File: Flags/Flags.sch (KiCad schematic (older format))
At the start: 35 parts, among them J1 Conn_01x09_Male, J2 Conn_01x12_Male, J3 Conn_01x04_Male, U1 74HC74, U2 74HC74, U3 74LS08, U4 74LS175, U5 74LS08

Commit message: Place ICs on Flags pcb
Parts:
- removed J2: Conn_01x12_Male, Connector_PinHeader_2.54mm:PinHeader_1x12_P2.54mm_Vertical, symbol Connector:Conn_01x12_Male
- added J2: Conn_01x07_Male, Connector_PinHeader_2.54mm:PinHeader_1x07_P2.54mm_Vertical, symbol Connector:Conn_01x07_Male
- added J4: Conn_01x05_Male, Connector_PinHeader_2.54mm:PinHeader_1x05_P2.54mm_Vertical, symbol Connector:Conn_01x05_Male
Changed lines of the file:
@@
-	1    0    0    -1
-$EndComp
-$Comp
-L Connector:Conn_01x12_Male J2
-U 1 1 62C30518
-P 1000 2750
-F 0 "J2" H 1075 3350 50  0000 C CNN
-F 1 "Conn_01x12_Male" H 875 2050 50  0000 C CNN
-F 2 "Connector_PinHeader_2.54mm:PinHeader_1x12_P2.54mm_Vertical" H 1000 2750 50  0001 C CNN
-F 3 "~" H 1000 2750 50  0001 C CNN
-	1    1000 2750
 	1    0    0    -1
 $EndComp
 Text Label 1200 2250 0    50   ~ 0
 CF_IN
+Text Label 1200 3400 0    50   ~ 0
+CF_EN
 Text Label 1200 2350 0    50   ~ 0
-CF_EN
+SF_IN
+Text Label 1200 3500 0    50   ~ 0
+SF_EN
 Text Label 1200 2450 0    50   ~ 0
-SF_IN
+ZF_IN
+Text Label 1200 3600 0    50   ~ 0
+ZF_EN
 Text Label 1200 2550 0    50   ~ 0
-SF_EN
+BF_IN
+Text Label 1200 3700 0    50   ~ 0
+BF_EN
+Text Label 1200 3800 0    50   ~ 0
+CMP_EN
 Text Label 1200 2650 0    50   ~ 0
-ZF_IN
+LT_IN
 Text Label 1200 2750 0    50   ~ 0
-ZF_EN
+~EQ_IN
 Text Label 1200 2850 0    50   ~ 0
-BF_IN
-Text Label 1200 2950 0    50   ~ 0
-BF_EN
-Text Label 1200 3350 0    50   ~ 0
-CMP_EN
-Text Label 1200 3050 0    50   ~ 0
-LT_IN
-Text Label 1200 3150 0    50   ~ 0
-~EQ_IN
-Text Label 1200 3250 0    50   ~ 0
 GT_IN
 $Comp
@@
 	1    0    0    -1
 $EndComp
+$Comp
+L Connector:Conn_01x05_Male J4
+U 1 1 62B6C12E
+P 1000 3600
+F 0 "J4" H 1108 3981 50  0000 C CNN
+F 1 "Conn_01x05_Male" H 1075 3325 50  0000 C CNN
+F 2 "Connector_PinHeader_2.54mm:PinHeader_1x05_P2.54mm_Vertical" H 1000 3600 50  0001 C CNN
+F 3 "~" H 1000 3600 50  0001 C CNN
+	1    1000 3600
+	1    0    0    -1
+$EndComp
+$Comp
+L Connector:Conn_01x07_Male J2
+U 1 1 62B72967
+P 1000 2550
+F 0 "J2" H 1108 3031 50  0000 C CNN
+F 1 "Conn_01x07_Male" H 1050 2175 50  0000 C CNN
+F 2 "Connector_PinHeader_2.54mm:PinHeader_1x07_P2.54mm_Vertical" H 1000 2550 50  0001 C CNN
+F 3 "~" H 1000 2550 50  0001 C CNN
+	1    1000 2550
+	1    0    0    -1
+$EndComp

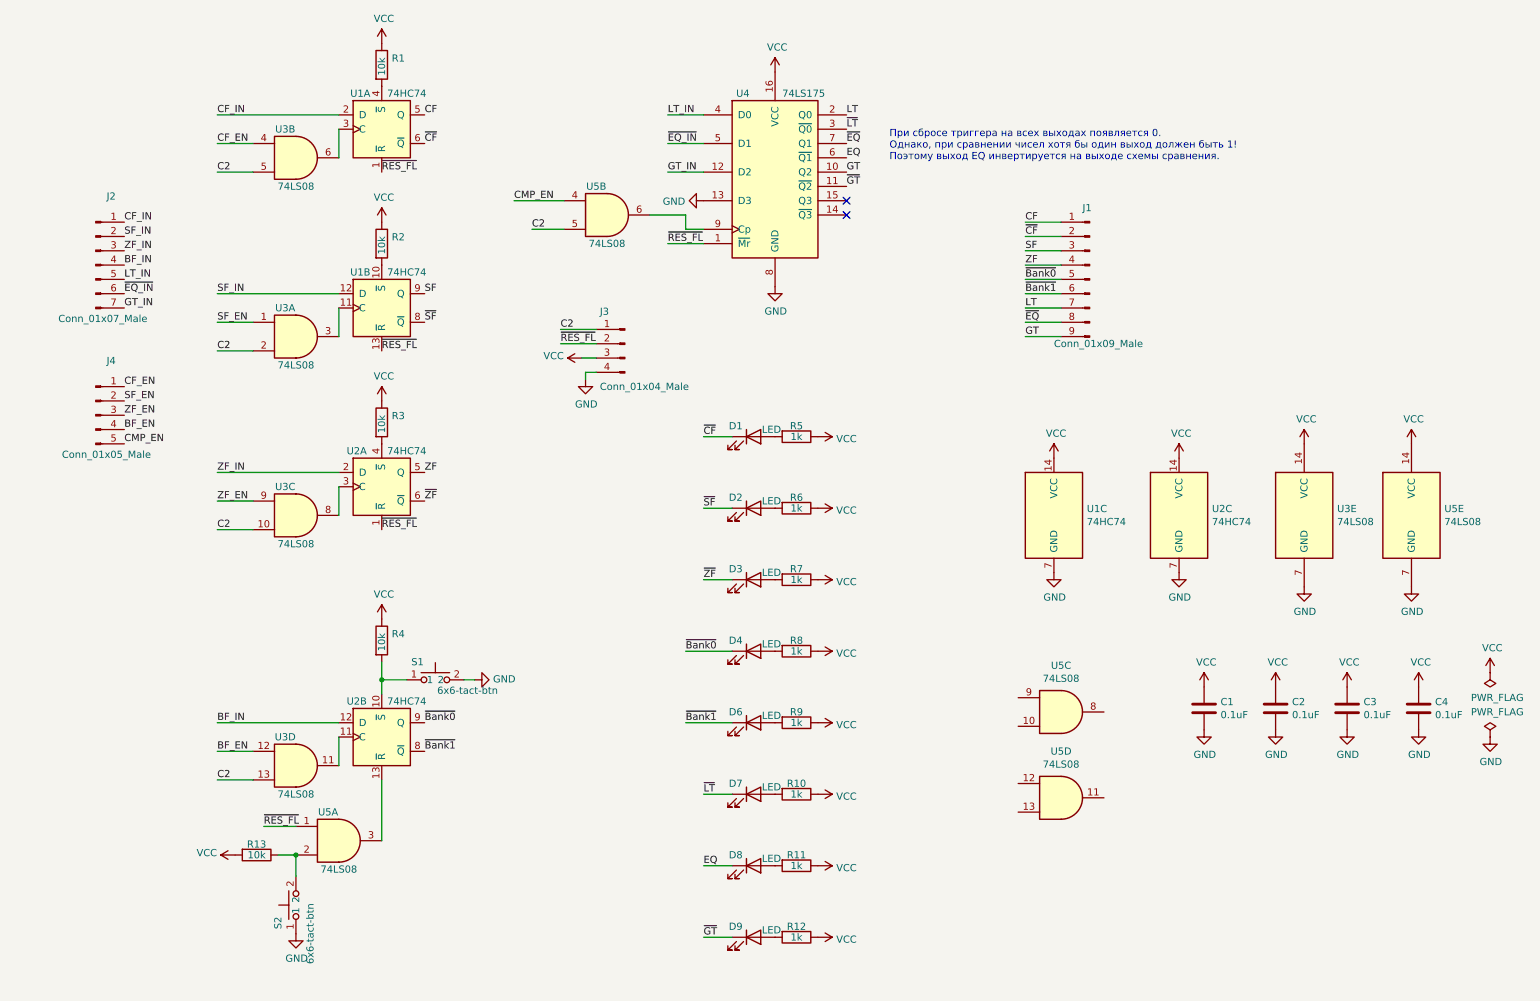
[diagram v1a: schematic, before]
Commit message: Remove some flags, fix board size
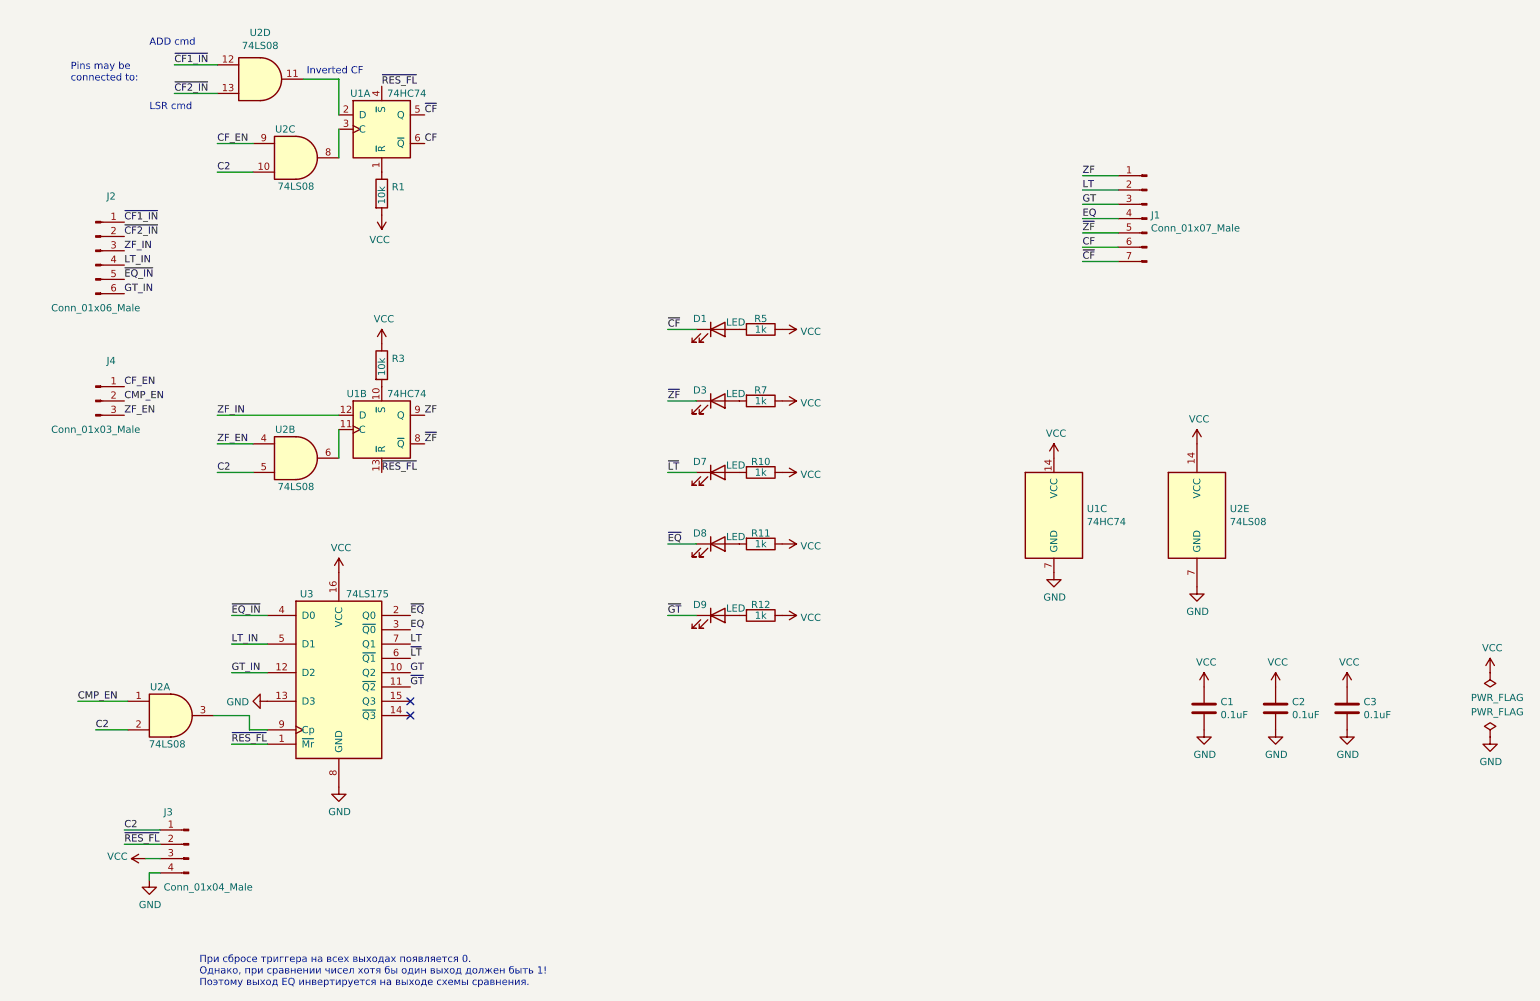
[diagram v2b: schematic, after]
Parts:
- removed C4: 0.1uF, Capacitor_THT:C_Disc_D5.0mm_W2.5mm_P5.00mm, symbol Device:C
- removed D2, D4, D6: LED, LED_THT:LED_Rectangular_W5.0mm_H2.0mm, symbol Device:LED
- removed J1: Conn_01x09_Male, Connector_PinHeader_2.54mm:PinHeader_1x09_P2.54mm_Vertical, symbol Connector:Conn_01x09_Male
- removed J2: Conn_01x07_Male, Connector_PinHeader_2.54mm:PinHeader_1x07_P2.54mm_Vertical, symbol Connector:Conn_01x07_Male
- removed J4: Conn_01x05_Male, Connector_PinHeader_2.54mm:PinHeader_1x05_P2.54mm_Vertical, symbol Connector:Conn_01x05_Male
- removed R13, R2, R4: 10k, Resistor_SMD:R_0805_2012Metric_Pad1.20x1.40mm_HandSolder, symbol Device:R
- removed R6, R8, R9: 1k, Resistor_SMD:R_0805_2012Metric_Pad1.20x1.40mm_HandSolder, symbol Device:R
- removed S1, S2: 6x6-tact-btn, Button_Switch_THT:SW_PUSH_6mm_H4.3mm, symbol CommonLibrary:6x6-tact-btn
- removed U2: 74HC74, Package_DIP:DIP-14_W7.62mm_Socket, symbol 74xx:74HC74
- removed unit 1 of U3
- removed unit 4 of U3
- removed unit 5 of U3
- removed unit 1 of U5
- removed unit 2 of U5
- removed unit 3 of U5
- removed unit 4 of U5
- added J1: Conn_01x07_Male, Connector_PinHeader_2.54mm:PinHeader_1x07_P2.54mm_Vertical, symbol Connector:Conn_01x07_Male
- added J2: Conn_01x06_Male, Connector_PinHeader_2.54mm:PinHeader_1x06_P2.54mm_Vertical, symbol Connector:Conn_01x06_Male
- added J4: Conn_01x03_Male, Connector_PinHeader_2.54mm:PinHeader_1x03_P2.54mm_Vertical, symbol Connector:Conn_01x03_Male
- added unit 1 of U2
- added unit 4 of U2
- renumbered U3 to U2, U5 to U2, U4 to U3
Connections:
- net SF is gone; now on net ZF: U1.9 (Q)
- net SF_IN is gone; now on net ZF_IN: U1.12 (D)
- net ~SF is gone; now on net ~ZF: U1.8 (~Q)
- net C2: now also U2.2
- net CF: now also U1.6 (~Q), J1.6 (Pin_6); no longer U1.5 (Q)
- net CF_EN: now also U2.9, J4.1 (Pin_1); no longer U2.4
- net CMP_EN: now also J4.2 (Pin_2), U2.1
- net EQ: now also U3.3 (~Q0), J1.4 (Pin_4); no longer D8.1 (K), U3.6 (~Q1)
- net GT: now also J1.3 (Pin_3)
- net GT_IN: now also J2.6 (Pin_6)
- net LT: now also U3.7 (Q1), J1.2 (Pin_2); no longer U3.2 (Q0)
- net LT_IN: now also U3.5 (D1), J2.4 (Pin_4); no longer U3.4 (D0)
- net VCC: now also R1.2; no longer R1.1
- net ZF: now also J1.1 (Pin_1)
- net ZF_EN: now also U2.4, J4.3 (Pin_3); no longer U2.9
- net ZF_IN: now also J2.3 (Pin_3)
- net ~CF: now also U1.5 (Q), J1.7 (Pin_7); no longer U1.6 (~Q)
- net ~EQ: now also D8.1 (K), U3.2 (Q0); no longer U3.7 (Q1)
- net ~EQ_IN: now also U3.4 (D0), J2.5 (Pin_5); no longer U3.5 (D1)
- net ~LT: now also U3.6 (~Q1); no longer U3.3 (~Q0)
- net ~RES_FL: now also U1.4 (~S); no longer U1.1 (~R)
- net ~ZF: now also J1.5 (Pin_5)
- net at U1.3 (C): now also U2.8; no longer U2.6
- net at U1.10 (~S): now also R3.2
- net at U1.11 (C): now also U2.6
- net at U3.9 (Cp): now also U2.3
- net CF_IN: no longer names the net of U1.2 (D)
- net CF_IN: now also U2.11
- new net: R1.1, U1.1 (~R)
- new net ~CF1_IN: J2.1 (Pin_1), U2.12
- new net ~CF2_IN: J2.2 (Pin_2), U2.13
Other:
- note added: "ADD cmd"
- note added: "Inverted CF"
- note added: "LSR cmd"
- note added: "Pins may be\nconnected to:"
- moved on the sheet: D1, D3, D7, D8, D9, J3, R1, R10, R11, R12, R3, R5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

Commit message: Flags pcb is ready
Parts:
- C1, C2: footprint Capacitor_THT:C_Disc_D5.0mm_W2.5mm_P5.00mm -> Capacitor_THT:C_Axial_L5.1mm_D3.1mm_P12.50mm_Horizontal
- C3: footprint Capacitor_THT:C_Disc_D5.0mm_W2.5mm_P5.00mm -> Capacitor_THT:C_Axial_L5.1mm_D3.1mm_P15.00mm_Horizontal
- R1, R3: footprint Resistor_SMD:R_0805_2012Metric_Pad1.20x1.40mm_HandSolder -> Resistor_THT:R_Axial_DIN0207_L6.3mm_D2.5mm_P7.62mm_Horizontal
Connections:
- net C2: now also J3.2 (Pin_2); no longer J3.1 (Pin_1)
- net LT_IN: now also J2.5 (Pin_5); no longer J2.4 (Pin_4)
- net ~CF: now also J1.5 (Pin_5); no longer J1.7 (Pin_7)
- net ~EQ_IN: now also J2.4 (Pin_4); no longer J2.5 (Pin_5)
- net ~RES_FL: now also J3.1 (Pin_1); no longer J3.2 (Pin_2)
- net ~ZF: now also J1.7 (Pin_7); no longer J1.5 (Pin_5)
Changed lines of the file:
@@
 F 0 "R1" H 3070 2096 50  0000 L CNN
 F 1 "10k" V 3000 1975 50  0000 L CNN
-F 2 "Resistor_SMD:R_0805_2012Metric_Pad1.20x1.40mm_HandSolder" V 2930 2050 50  0001 C CNN
+F 2 "Resistor_THT:R_Axial_DIN0207_L6.3mm_D2.5mm_P7.62mm_Horizontal" V 2930 2050 50  0001 C CNN
 F 3 "~" H 3000 2050 50  0001 C CNN
 	1    3000 2050
@@
 F 0 "R3" H 3070 3296 50  0000 L CNN
 F 1 "10k" V 3000 3175 50  0000 L CNN
-F 2 "Resistor_SMD:R_0805_2012Metric_Pad1.20x1.40mm_HandSolder" V 2930 3250 50  0001 C CNN
+F 2 "Resistor_THT:R_Axial_DIN0207_L6.3mm_D2.5mm_P7.62mm_Horizontal" V 2930 3250 50  0001 C CNN
 F 3 "~" H 3000 3250 50  0001 C CNN
 	1    3000 3250
@@
 F 0 "C1" H 8865 5696 50  0000 L CNN
 F 1 "0.1uF" H 8865 5605 50  0000 L CNN
-F 2 "Capacitor_THT:C_Disc_D5.0mm_W2.5mm_P5.00mm" H 8788 5500 50  0001 C CNN
+F 2 "Capacitor_THT:C_Axial_L5.1mm_D3.1mm_P12.50mm_Horizontal" H 8788 5500 50  0001 C CNN
 F 3 "~" H 8750 5650 50  0001 C CNN
 	1    8750 5650
@@
 F 0 "C2" H 9365 5696 50  0000 L CNN
 F 1 "0.1uF" H 9365 5605 50  0000 L CNN
-F 2 "Capacitor_THT:C_Disc_D5.0mm_W2.5mm_P5.00mm" H 9288 5500 50  0001 C CNN
+F 2 "Capacitor_THT:C_Axial_L5.1mm_D3.1mm_P12.50mm_Horizontal" H 9288 5500 50  0001 C CNN
 F 3 "~" H 9250 5650 50  0001 C CNN
 	1    9250 5650
@@
 F 0 "C3" H 9865 5696 50  0000 L CNN
 F 1 "0.1uF" H 9865 5605 50  0000 L CNN
-F 2 "Capacitor_THT:C_Disc_D5.0mm_W2.5mm_P5.00mm" H 9788 5500 50  0001 C CNN
+F 2 "Capacitor_THT:C_Axial_L5.1mm_D3.1mm_P15.00mm_Horizontal" H 9788 5500 50  0001 C CNN
 F 3 "~" H 9750 5650 50  0001 C CNN
 	1    9750 5650
@@
 Text Label 1200 3500 0    50   ~ 0
 CMP_EN
+Text Label 1200 2650 0    50   ~ 0
+LT_IN
 Text Label 1200 2550 0    50   ~ 0
-LT_IN
-Text Label 1200 2650 0    50   ~ 0
 ~EQ_IN
 Text Label 1200 2750 0    50   ~ 0
@@
 Text Label 7900 2425 0    50   ~ 0
 CF
-Text Label 7900 2525 0    50   ~ 0
+Text Label 7900 2325 0    50   ~ 0
 ~CF
 Text Label 7900 1925 0    50   ~ 0
@@
 Wire Wire Line
 	1200 6600 1450 6600
+Text Label 1200 6600 0    50   ~ 0
+C2
 Text Label 1200 6500 0    50   ~ 0
-C2
-Text Label 1200 6600 0    50   ~ 0
 ~RES_FL
 $Comp
@@
 	1    0    0    -1
 $EndComp
-Text Label 7900 2325 0    50   ~ 0
+Text Label 7900 2525 0    50   ~ 0
 ~ZF
 $Comp

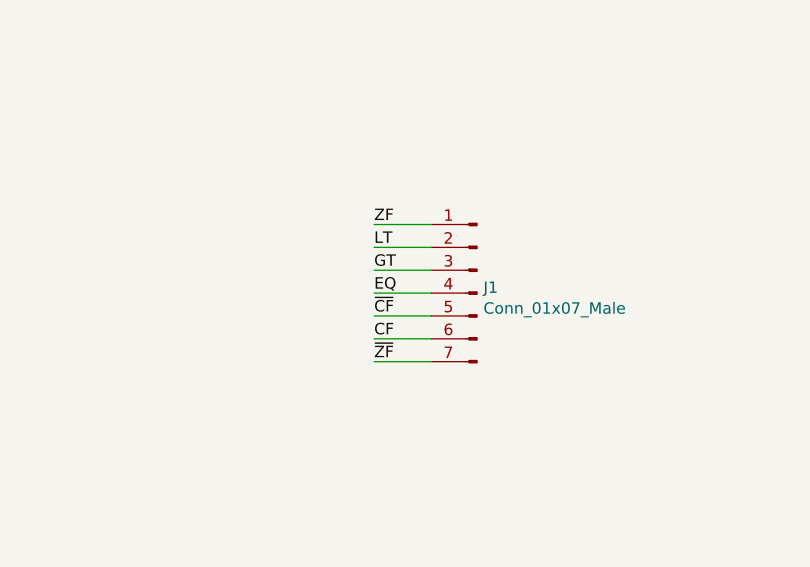
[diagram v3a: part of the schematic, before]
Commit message: Move ZF output to another place
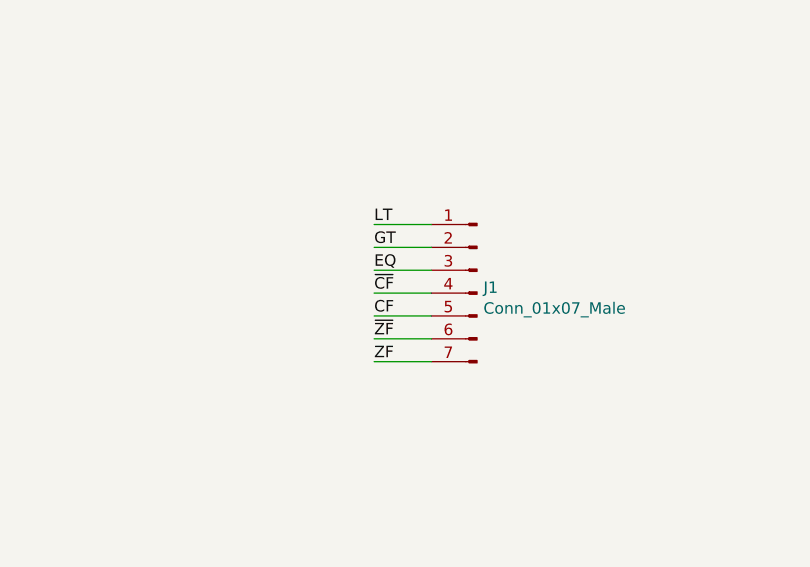
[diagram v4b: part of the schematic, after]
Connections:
- net CF: now also J1.5 (Pin_5); no longer J1.6 (Pin_6)
- net EQ: now also J1.3 (Pin_3); no longer J1.4 (Pin_4)
- net GT: now also J1.2 (Pin_2); no longer J1.3 (Pin_3)
- net LT: now also J1.1 (Pin_1); no longer J1.2 (Pin_2)
- net ZF: now also J1.7 (Pin_7); no longer J1.1 (Pin_1)
- net ~CF: now also J1.4 (Pin_4); no longer J1.5 (Pin_5)
- net ~ZF: now also J1.6 (Pin_6); no longer J1.7 (Pin_7)
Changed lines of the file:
@@
 GT_IN
+Wire Wire Line
+	7900 2325 8150 2325
 Wire Wire Line
 	7900 2425 8150 2425
@@
 	7900 2525 8150 2525
 Wire Wire Line
+	7900 2225 8150 2225
+Wire Wire Line
 	7900 1925 8150 1925
 Wire Wire Line
-	7900 2325 8150 2325
+	7900 2125 8150 2125
 Wire Wire Line
 	7900 2025 8150 2025
-Wire Wire Line
-	7900 2225 8150 2225
-Wire Wire Line
-	7900 2125 8150 2125
+Text Label 7900 2025 0    50   ~ 0
+GT
 Text Label 7900 2125 0    50   ~ 0
-GT
+EQ
+Text Label 7900 1925 0    50   ~ 0
+LT
+Text Label 7900 2325 0    50   ~ 0
+CF
 Text Label 7900 2225 0    50   ~ 0
-EQ
-Text Label 7900 2025 0    50   ~ 0
-LT
-Text Label 7900 2425 0    50   ~ 0
-CF
-Text Label 7900 2325 0    50   ~ 0
 ~CF
-Text Label 7900 1925 0    50   ~ 0
+Text Label 7900 2525 0    50   ~ 0
 ZF
 $Comp
@@
 	1    0    0    -1
 $EndComp
-Text Label 7900 2525 0    50   ~ 0
+Text Label 7900 2425 0    50   ~ 0
 ~ZF
 $Comp

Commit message: Polishing Flags
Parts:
- renumbered D3 to D2, D7 to D3, D8 to D4, D9 to D5, J4 to J3, J3 to J4, R5 to R2, R7 to R4, R10 to R5, R11 to R6, R12 to R7, U2 to U1, U1 to U2
